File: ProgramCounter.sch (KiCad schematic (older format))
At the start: 22 parts, among them U10 74LS163, U11 74LS163, U12 74LS541

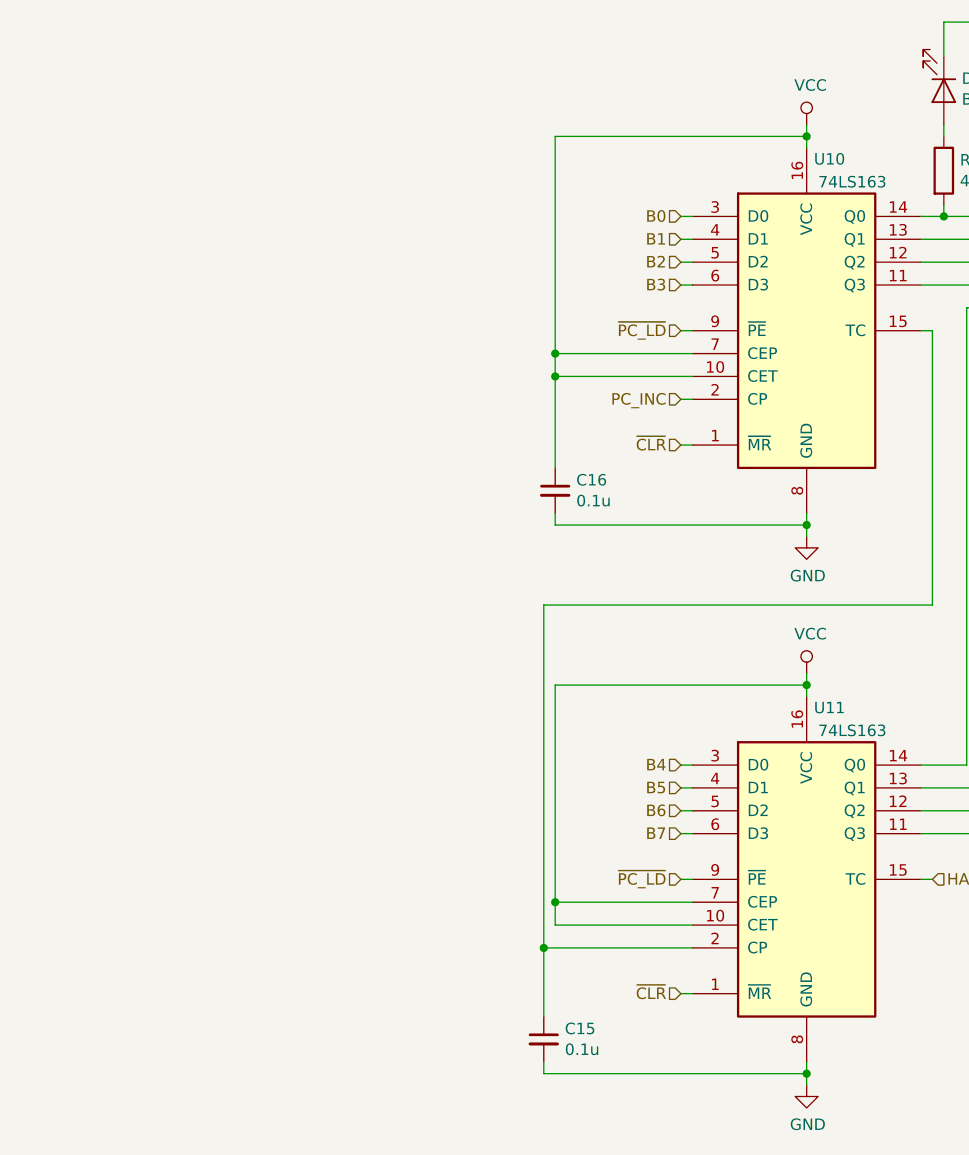
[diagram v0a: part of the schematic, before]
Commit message: Fixed second Program Counter.
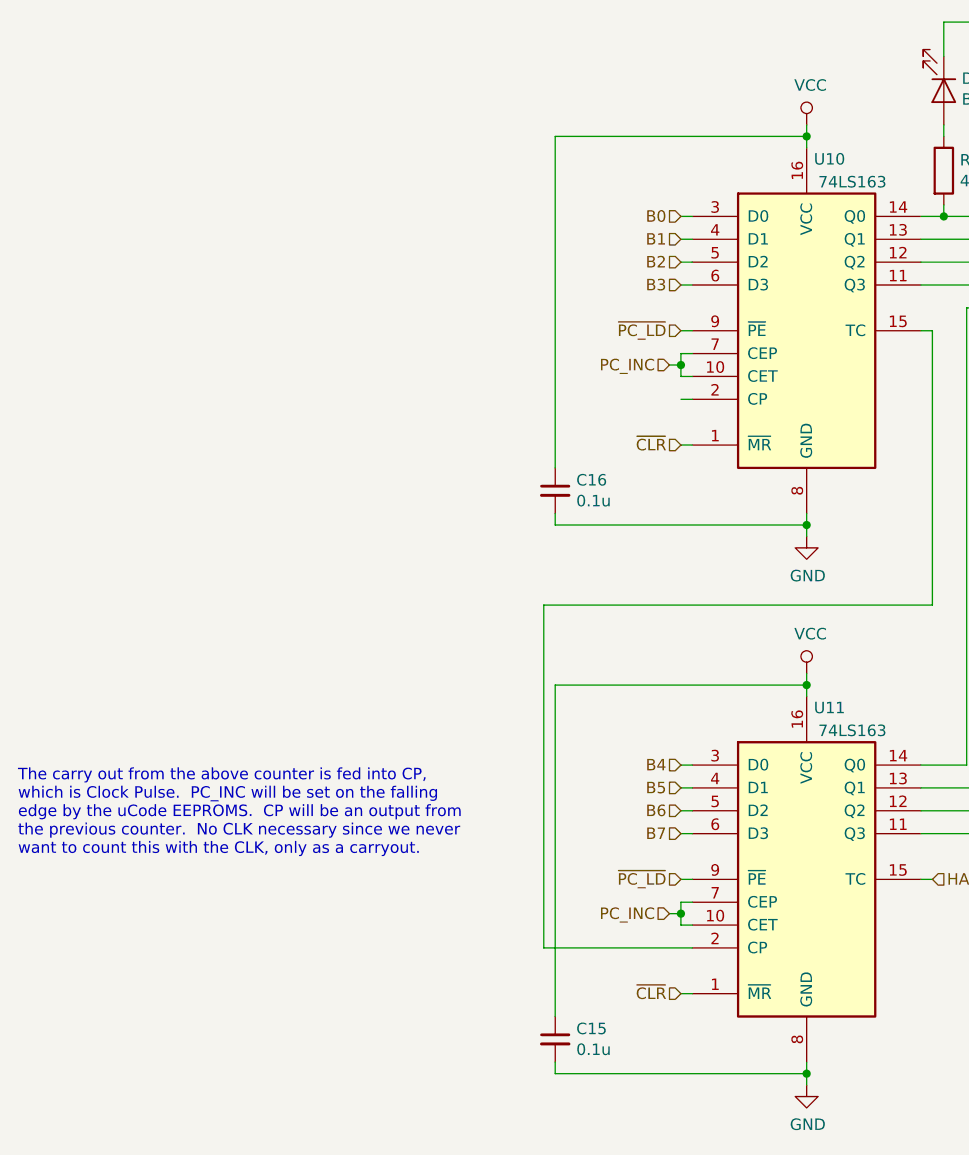
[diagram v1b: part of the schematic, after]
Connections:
- net PC_INC: now also U10.10 (CET), U10.7 (CEP), U11.10 (CET), U11.7 (CEP); no longer U10.2 (CP)
- net VCC: now also C15.1; no longer U10.10 (CET), U10.7 (CEP), U11.10 (CET), U11.7 (CEP)
- net at U10.15 (TC), U11.2 (CP): no longer C15.1
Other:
- note added: "The carry out from the above counter is fed into CP,\nwhich is Clock Pulse. PC_INC will be set on the falling\nedge by the uCode EEPROMS. CP will be an output from \nthe previous counter. No CLK necessary since we never\nwant to count this with the CLK, only as a carryout."
- moved on the sheet: C15
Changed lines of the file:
@@
 $Descr A4 11693 8268
 encoding utf-8
-Sheet 5 8
+Sheet 8 8
 Title ""
 Date ""
@@
 Wire Wire Line
 	4900 2250 3800 2250
-Wire Wire Line
-	3800 2250 3800 3200
-Wire Wire Line
-	3800 3200 4400 3200
 Connection ~ 4900 2250
 Wire Wire Line
 	4900 2250 4900 2300
-Wire Wire Line
-	3800 3200 3800 3300
-Wire Wire Line
-	3800 3300 4400 3300
-Connection ~ 3800 3200
 Text HLabel 4350 2600 0    50   Input ~ 0
 B0
@@
 	5450 4300 3750 4300
 Wire Wire Line
-	3750 4300 3750 5800
-Wire Wire Line
-	3750 5800 4400 5800
-Wire Wire Line
 	4900 4600 4900 4650
 Wire Wire Line
@@
 Wire Wire Line
 	4900 4650 3800 4650
-Wire Wire Line
-	3800 4650 3800 5600
-Wire Wire Line
-	3800 5600 4400 5600
 Connection ~ 4900 4650
 Wire Wire Line
 	4900 4650 4900 4700
-Wire Wire Line
-	3800 5600 3800 5700
-Wire Wire Line
-	3800 5700 4400 5700
-Connection ~ 3800 5600
-Text HLabel 4350 3400 0    50   Input ~ 0
+Text HLabel 4300 3250 0    50   Input ~ 0
 PC_INC
 Text HLabel 4350 3100 0    50   Input ~ 0
 ~PC_LD
-Text HLabel 4350 3600 0    50   Input ~ 0
-~CLR
-Text HLabel 4350 5500 0    50   Input ~ 0
-~PC_LD
-Text HLabel 4350 6000 0    50   Input ~ 0
-~CLR
 $Comp
 L Device:C_Small C16
@@
 	1    0    0    -1
 $EndComp
-$Comp
-L Device:C_Small C15
-U 1 1 5F3A023B
-P 3750 6200
-F 0 "C15" H 3842 6246 50  0000 L CNN
-F 1 "0.1u" H 3842 6155 50  0000 L CNN
-F 2 "" H 3750 6200 50  0001 C CNN
-F 3 "~" H 3750 6200 50  0001 C CNN
-	1    3750 6200
-	1    0    0    -1
-$EndComp
-Wire Wire Line
-	3750 5800 3750 6100
-Connection ~ 3750 5800
-Wire Wire Line
-	3800 3700 3800 3300
-Connection ~ 3800 3300
 Wire Wire Line
 	3800 3900 3800 3950
@@
 Wire Wire Line
 	4900 3950 4900 4000
-Wire Wire Line
-	3750 6300 3750 6350
-Wire Wire Line
-	3750 6350 4900 6350
-Wire Wire Line
-	4900 6350 4900 6300
 $Comp
 L power:GND #PWR026
@@
 $EndComp
 Wire Wire Line
-	4900 6400 4900 6350
-Connection ~ 4900 6350
-Wire Wire Line
 	5400 5000 5600 5000
 Wire Wire Line
@@
 	1    0    0    -1
 $EndComp
+Text HLabel 4350 6000 0    50   Input ~ 0
+~CLR
+Text HLabel 4350 3600 0    50   Input ~ 0
+~CLR
+Wire Wire Line
+	3800 2250 3800 3700
+Wire Wire Line
+	4300 3250 4350 3250
+Wire Wire Line
+	4350 3250 4350 3200
+Wire Wire Line
+	4350 3200 4400 3200
+Wire Wire Line
+	4350 3250 4350 3300
+Wire Wire Line
+	4350 3300 4400 3300
+Connection ~ 4350 3250
+Wire Wire Line
+	3750 4300 3750 5800
+Wire Wire Line
+	3750 5800 4400 5800
+Text HLabel 4350 5500 0    50   Input ~ 0
+~PC_LD
+$Comp
+L Device:C_Small C15
+U 1 1 5F3A023B
+P 3800 6200
+F 0 "C15" H 3892 6246 50  0000 L CNN
+F 1 "0.1u" H 3892 6155 50  0000 L CNN
+F 2 "" H 3800 6200 50  0001 C CNN
+F 3 "~" H 3800 6200 50  0001 C CNN
+	1    3800 6200
+	1    0    0    -1
+$EndComp
+Wire Wire Line
+	4900 6300 4900 6350
+Wire Wire Line
+	3800 6300 3800 6350
+Wire Wire Line
+	3800 6350 4900 6350
+Connection ~ 4900 6350
+Wire Wire Line
+	4900 6350 4900 6400
+Wire Wire Line
+	3800 4650 3800 6100
+Text HLabel 4300 5650 0    50   Input ~ 0
+PC_INC
+Wire Wire Line
+	4300 5650 4350 5650
+Wire Wire Line
+	4350 5650 4350 5700
+Wire Wire Line
+	4350 5700 4400 5700
+Wire Wire Line
+	4350 5650 4350 5600
+Wire Wire Line
+	4350 5600 4400 5600
+Connection ~ 4350 5650
+Text Notes 1450 5400 0    50   ~ 0
+The carry out from the above counter is fed into CP,\nwhich is Clock Pulse.  PC_INC will be set on the falling\nedge by the uCode EEPROMS.  CP will be an output from \nthe previous counter.  No CLK necessary since we never\nwant to count this with the CLK, only as a carryout.
 $EndSCHEMATC

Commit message: Continued work.  Pushing for remote work.
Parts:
- U10, U11: value 74LS163 -> 74HC161
- U12: value 74LS541 -> 74HC541
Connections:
- net PC_INC: no longer U11.10 (CET), U11.7 (CEP)
- net at U10.15 (TC): now also U11.10 (CET), U11.7 (CEP); no longer U11.2 (CP)
- net CLK: now reaches U10.2 (CP)
- net CLK: now also U11.2 (CP)
- net HALT renamed TR_HALT
- net ~PC_LD renamed ~PC_IN
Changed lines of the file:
@@
 $Descr A4 11693 8268
 encoding utf-8
-Sheet 8 8
+Sheet 7 9
 Title ""
 Date ""
@@
 P 4900 5500
 F 0 "U11" H 5000 6250 50  0000 C CNN
-F 1 "74LS163" H 5100 6150 50  0000 C CNN
+F 1 "74HC161" H 5100 6150 50  0000 C CNN
 F 2 "" H 4900 5500 50  0001 C CNN
 F 3 "http://www.ti.com/lit/gpn/sn74LS163" H 4900 5500 50  0001 C CNN
@@
 Wire Wire Line
 	4900 3900 4900 3950
-Text HLabel 8700 2600 2    50   Input ~ 0
+Text HLabel 8700 2600 2    50   Output ~ 0
 B0
-Text HLabel 8700 2700 2    50   Input ~ 0
+Text HLabel 8700 2700 2    50   Output ~ 0
 B1
-Text HLabel 8700 2800 2    50   Input ~ 0
+Text HLabel 8700 2800 2    50   Output ~ 0
 B2
-Text HLabel 8700 2900 2    50   Input ~ 0
+Text HLabel 8700 2900 2    50   Output ~ 0
 B3
-Text HLabel 8700 3000 2    50   Input ~ 0
+Text HLabel 8700 3000 2    50   Output ~ 0
 B4
-Text HLabel 8700 3100 2    50   Input ~ 0
+Text HLabel 8700 3100 2    50   Output ~ 0
 B5
-Text HLabel 8700 3200 2    50   Input ~ 0
+Text HLabel 8700 3200 2    50   Output ~ 0
 B6
-Text HLabel 8700 3300 2    50   Input ~ 0
+Text HLabel 8700 3300 2    50   Output ~ 0
 B7
 $Comp
@@
 PC_INC
 Text HLabel 4350 3100 0    50   Input ~ 0
-~PC_LD
+~PC_IN
 $Comp
 L Device:C_Small C16
@@
 	7650 3600 7700 3600
 Connection ~ 7650 3550
-Text HLabel 5450 5500 2    50   Input ~ 0
-HALT
+Text HLabel 5450 5500 2    50   Output ~ 0
+TR_HALT
 Wire Wire Line
 	5400 5500 5450 5500
@@
 P 4900 3100
 F 0 "U10" H 5000 3850 50  0000 C CNN
-F 1 "74LS163" H 5100 3750 50  0000 C CNN
+F 1 "74HC161" H 5100 3750 50  0000 C CNN
 F 2 "" H 4900 3100 50  0001 C CNN
 F 3 "http://www.ti.com/lit/gpn/sn74LS163" H 4900 3100 50  0001 C CNN
@@
 P 8200 3100
 F 0 "U12" H 8300 3850 50  0000 C CNN
-F 1 "74LS541" H 8400 3750 50  0000 C CNN
+F 1 "74HC541" H 8400 3750 50  0000 C CNN
 F 2 "" H 8200 3100 50  0001 C CNN
 F 3 "http://www.ti.com/lit/gpn/sn74LS541" H 8200 3100 50  0001 C CNN
@@
 	4350 3300 4400 3300
 Connection ~ 4350 3250
-Wire Wire Line
-	3750 4300 3750 5800
-Wire Wire Line
-	3750 5800 4400 5800
 Text HLabel 4350 5500 0    50   Input ~ 0
-~PC_LD
+~PC_IN
 $Comp
 L Device:C_Small C15
@@
 Wire Wire Line
 	3800 4650 3800 6100
-Text HLabel 4300 5650 0    50   Input ~ 0
-PC_INC
-Wire Wire Line
-	4300 5650 4350 5650
-Wire Wire Line
-	4350 5650 4350 5700
-Wire Wire Line
-	4350 5700 4400 5700
-Wire Wire Line
-	4350 5650 4350 5600
-Wire Wire Line
-	4350 5600 4400 5600
-Connection ~ 4350 5650
 Text Notes 1450 5400 0    50   ~ 0
 The carry out from the above counter is fed into CP,\nwhich is Clock Pulse.  PC_INC will be set on the falling\nedge by the uCode EEPROMS.  CP will be an output from \nthe previous counter.  No CLK necessary since we never\nwant to count this with the CLK, only as a carryout.
+Text HLabel 4350 3400 0    50   Input ~ 0
+CLK
+Wire Wire Line
+	3750 4300 3750 5650
+Wire Wire Line
+	3750 5650 4350 5650
+Wire Wire Line
+	4350 5650 4350 5600
+Wire Wire Line
+	4350 5600 4400 5600
+Wire Wire Line
+	4350 5650 4350 5700
+Wire Wire Line
+	4350 5700 4400 5700
+Connection ~ 4350 5650
+Wire Wire Line
+	4350 5800 4400 5800
+Text HLabel 4350 5800 0    50   Input ~ 0
+CLK
 $EndSCHEMATC

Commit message: For desktop work
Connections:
- net ~CLR renamed ~RST
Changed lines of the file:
@@
 $Descr A4 11693 8268
 encoding utf-8
-Sheet 7 9
+Sheet 9 9
 Title ""
 Date ""
@@
 $EndComp
 Text HLabel 4350 6000 0    50   Input ~ 0
-~CLR
+~RST
 Text HLabel 4350 3600 0    50   Input ~ 0
-~CLR
+~RST
 Wire Wire Line
 	3800 2250 3800 3700

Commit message: Migrated old device part numbers to SN74 LS or HCT series
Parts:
- U10, U11: value 74HC161 -> 74LS161AN
- U12: value 74HC541 -> 74HCT541N
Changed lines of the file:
@@
 P 4900 5500
 F 0 "U11" H 5000 6250 50  0000 C CNN
-F 1 "74HC161" H 5100 6150 50  0000 C CNN
+F 1 "74LS161AN" H 5150 6150 50  0000 C CNN
 F 2 "" H 4900 5500 50  0001 C CNN
 F 3 "http://www.ti.com/lit/gpn/sn74LS163" H 4900 5500 50  0001 C CNN
@@
 P 4900 3100
 F 0 "U10" H 5000 3850 50  0000 C CNN
-F 1 "74HC161" H 5100 3750 50  0000 C CNN
+F 1 "74LS161AN" H 5150 3750 50  0000 C CNN
 F 2 "" H 4900 3100 50  0001 C CNN
 F 3 "http://www.ti.com/lit/gpn/sn74LS163" H 4900 3100 50  0001 C CNN
@@
 P 8200 3100
 F 0 "U12" H 8300 3850 50  0000 C CNN
-F 1 "74HC541" H 8400 3750 50  0000 C CNN
+F 1 "74HCT541N" H 8450 3750 50  0000 C CNN
 F 2 "" H 8200 3100 50  0001 C CNN
 F 3 "http://www.ti.com/lit/gpn/sn74LS541" H 8200 3100 50  0001 C CNN

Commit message: Remote work
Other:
- note added: "Program Counter\n(up only)"
- note added: "Program Counter\nBus Buffer"
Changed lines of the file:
@@
 $Descr A4 11693 8268
 encoding utf-8
-Sheet 9 9
+Sheet 8 9
 Title ""
 Date ""
@@
 L power:GND #PWR029
 U 1 1 5F4B1E72
-P 7900 1800
-F 0 "#PWR029" H 7900 1550 50  0001 C CNN
-F 1 "GND" H 7905 1627 50  0000 C CNN
-F 2 "" H 7900 1800 50  0001 C CNN
-F 3 "" H 7900 1800 50  0001 C CNN
-	1    7900 1800
-	1    0    0    -1
-$EndComp
-Wire Wire Line
-	7900 1800 7900 1750
-Wire Wire Line
-	7900 1750 7600 1750
+P 7950 1800
+F 0 "#PWR029" H 7950 1550 50  0001 C CNN
+F 1 "GND" H 7955 1627 50  0000 C CNN
+F 2 "" H 7950 1800 50  0001 C CNN
+F 3 "" H 7950 1800 50  0001 C CNN
+	1    7950 1800
+	1    0    0    -1
+$EndComp
+Wire Wire Line
+	7950 1800 7950 1750
+Wire Wire Line
+	7950 1750 7600 1750
 Wire Wire Line
 	5500 1750 5500 1900
@@
 Text HLabel 4350 5800 0    50   Input ~ 0
 CLK
+Text Notes 3475 3850 2    118  ~ 0
+Program Counter\n(up only)
+Text Notes 9250 3250 0    118  ~ 0
+Program Counter\nBus Buffer
 $EndSCHEMATC

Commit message: Replaced all broken schematics with the up-to-date versions.  Some symbols missing.  This version will be the one created IRL except for the carry flag.
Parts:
- added C803, C804, C806: 0.1u, symbol Breadboard_CPU-rescue:C_Small-Device
- added D802, D804, D806, D808, D810, D812, D814, D816: Blue, symbol Breadboard_CPU-rescue:LED-Device
- added R802, R804, R806, R808, R810, R812, R814, R816: 4.7k, symbol Breadboard_CPU-rescue:R-Device
- added U801: 74HCT08N, symbol Breadboard_CPU-rescue:74LS08-74xx
- added U802: 74HCT74N, symbol Breadboard_CPU-rescue:74LS74-74xx
- added U803: 74LS32, symbol Breadboard_CPU-rescue:74LS32-74xx
- added U806, U807: 74LS161AN, symbol Breadboard_CPU-rescue:74LS163-74xx
- added U809: 74HCT541N, symbol Breadboard_CPU-rescue:74LS541-74xx
- C801: renamed from C16; symbol Device:C_Small -> Breadboard_CPU-rescue:C_Small-Device
- C802: renamed from C15; symbol Device:C_Small -> Breadboard_CPU-rescue:C_Small-Device
- C805: renamed from C17; symbol Device:C_Small -> Breadboard_CPU-rescue:C_Small-Device
- D801: renamed from D6; symbol Device:LED -> Breadboard_CPU-rescue:LED-Device
- D803: renamed from D7; symbol Device:LED -> Breadboard_CPU-rescue:LED-Device
- D805: renamed from D8; symbol Device:LED -> Breadboard_CPU-rescue:LED-Device
- D807: renamed from D9; symbol Device:LED -> Breadboard_CPU-rescue:LED-Device
- D809: renamed from D10; symbol Device:LED -> Breadboard_CPU-rescue:LED-Device
- D811: renamed from D11; symbol Device:LED -> Breadboard_CPU-rescue:LED-Device
- D813: renamed from D12; symbol Device:LED -> Breadboard_CPU-rescue:LED-Device
- D815: renamed from D13; symbol Device:LED -> Breadboard_CPU-rescue:LED-Device
- R801: renamed from R12; symbol Device:R -> Breadboard_CPU-rescue:R-Device
- R803: renamed from R13; symbol Device:R -> Breadboard_CPU-rescue:R-Device
- R805: renamed from R14; symbol Device:R -> Breadboard_CPU-rescue:R-Device
- R807: renamed from R15; symbol Device:R -> Breadboard_CPU-rescue:R-Device
- R809: renamed from R16; symbol Device:R -> Breadboard_CPU-rescue:R-Device
- R811: renamed from R17; symbol Device:R -> Breadboard_CPU-rescue:R-Device
- R813: renamed from R18; symbol Device:R -> Breadboard_CPU-rescue:R-Device
- R815: renamed from R19; symbol Device:R -> Breadboard_CPU-rescue:R-Device
- U804: renamed from U10; symbol 74xx:74LS163 -> Breadboard_CPU-rescue:74LS163-74xx
- U805: renamed from U11; symbol 74xx:74LS163 -> Breadboard_CPU-rescue:74LS163-74xx
- U808: renamed from U12; symbol 74xx:74LS541 -> Breadboard_CPU-rescue:74LS541-74xx
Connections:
- net B0: now also U806.3 (D0), U809.18 (Y0)
- net B1: now also U806.4 (D1), U809.17 (Y1)
- net B2: now also U806.5 (D2), U809.16 (Y2)
- net B3: now also U806.6 (D3), U809.15 (Y3)
- net B4: now also U807.3 (D0), U809.14 (Y4)
- net B5: now also U807.4 (D1), U809.13 (Y5)
- net B6: now also U807.5 (D2), U809.12 (Y6)
- net B7: now also U807.6 (D3), U809.11 (Y7)
- net CLK: now also U806.2 (CP), U807.2 (CP)
- net GND: now also C803.2, C804.2, C806.2, D802.1 (K), D804.1 (K), D806.1 (K), D808.1 (K), D810.1 (K), D812.1 (K), D814.1 (K), D816.1 (K), U801.7 (GND), U802.7 (GND), U803.7 (GND), U806.8 (GND), U807.8 (GND), U809.10 (GND)
- net VCC: now also C803.1, C804.1, C806.1, U801.14 (VCC), U802.10 (~S), U802.14 (VCC), U802.4 (~S), U803.14 (VCC), U806.16 (VCC), U807.16 (VCC), U809.20 (VCC)
- net ~PC_IN: now also U803.2, U803.5; no longer U804.9 (~PE), U805.9 (~PE)
- net ~PC_OUT: now also U803.12, U803.9; no longer U808.1 (G1), U808.19 (G2)
- net ~RST: now also U802.1 (~R), U802.13 (~R), U806.1 (~MR), U807.1 (~MR)
- net TR_HALT: no longer names the net of U805.15 (TC)
- net TR_HALT: now also U806.10 (CET), U806.7 (CEP)
- new net: U803.3, U804.9 (~PE), U805.9 (~PE)
- new net: U803.8, U808.1 (G1), U808.19 (G2)
- new net: U801.11, U802.3 (C)
- new net: U801.8, U802.11 (C)
- new net: U803.6, U806.9 (~PE), U807.9 (~PE)
- new net: U803.11, U809.1 (G1), U809.19 (G2)
- new net: U806.15 (TC), U807.10 (CET), U807.7 (CEP)
- new net: R816.2, U807.11 (Q3), U809.9 (A7)
- new net: R814.2, U807.12 (Q2), U809.8 (A6)
- new net: R812.2, U807.13 (Q1), U809.7 (A5)
- new net: R810.2, U807.14 (Q0), U809.6 (A4)
- new net: R808.2, U806.11 (Q3), U809.5 (A3)
- new net: R806.2, U806.12 (Q2), U809.4 (A2)
- new net: R804.2, U806.13 (Q1), U809.3 (A1)
- new net: R802.2, U806.14 (Q0), U809.2 (A0)
- new net: D802.2 (A), R802.1
- new net: D804.2 (A), R804.1
- new net: D806.2 (A), R806.1
- new net: D808.2 (A), R808.1
- new net: D810.2 (A), R810.1
- new net: D812.2 (A), R812.1
- new net: D814.2 (A), R814.1
- new net: D816.2 (A), R816.1
- new net PC_IN: U801.12
- new net PC_OUT: U801.9
- new net ~CLK: U801.10, U801.13
- new net ~PC_EN_LD_HIGH: U802.5 (Q), U803.4
- new net ~PC_EN_LD_LOW: U802.2 (D), U802.6 (~Q), U803.1
- new net ~PC_EN_OUT_HIGH: U802.9 (Q), U803.13
- new net ~PC_EN_OUT_LOW: U802.12 (D), U802.8 (~Q), U803.10
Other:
- note removed: "The carry out from the above counter is fed into CP,\nwhich is Clock Pulse. PC_INC will be set on the falling\nedge by the uCode EEPROMS. CP will be an output from \nthe previous counter. No CLK necessary since we never\nwant to count this with the CLK, only as a carryout."
- moved on the sheet: C801, C802, C805, D801, D803, D805, D807, D809, D811, D813, D815, R801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

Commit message: Libraries re-imported.  Using rescue symbols still.  Adjusted multi-byte registers to use low-byte first.. applied this convention to all multi-byte registers for consistency.
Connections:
- net ~PC_EN_LD_HIGH: now also U802.2 (D), U802.6 (~Q); no longer U802.5 (Q)
- net ~PC_EN_LD_LOW: now also U802.5 (Q); no longer U802.2 (D), U802.6 (~Q)
- net ~PC_EN_OUT_HIGH: now also U802.12 (D), U802.8 (~Q); no longer U802.9 (Q)
- net ~PC_EN_OUT_LOW: now also U802.9 (Q); no longer U802.12 (D), U802.8 (~Q)
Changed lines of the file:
@@
 Wire Wire Line
 	3425 5375 3475 5375
+Text Label 3475 5575 0    50   ~ 0
+~PC_EN_LD_HIGH
 Text Label 3475 5375 0    50   ~ 0
-~PC_EN_LD_HIGH
-Text Label 3475 5575 0    50   ~ 0
 ~PC_EN_LD_LOW
 Wire Wire Line
@@
 Wire Wire Line
 	3425 6650 3475 6650
+Text Label 3475 6850 0    50   ~ 0
+~PC_EN_OUT_HIGH
 Text Label 3475 6650 0    50   ~ 0
-~PC_EN_OUT_HIGH
-Text Label 3475 6850 0    50   ~ 0
 ~PC_EN_OUT_LOW
 Text HLabel 2075 5575 0    50   Input ~ 0
